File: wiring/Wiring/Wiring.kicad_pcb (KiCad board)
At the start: 2 copper layers, 21 parts, among them U1 MAIN, U2 E, U3 A, U3 B, U3 C, U3 D, U3 F, U3 H, U3 I, U3 J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

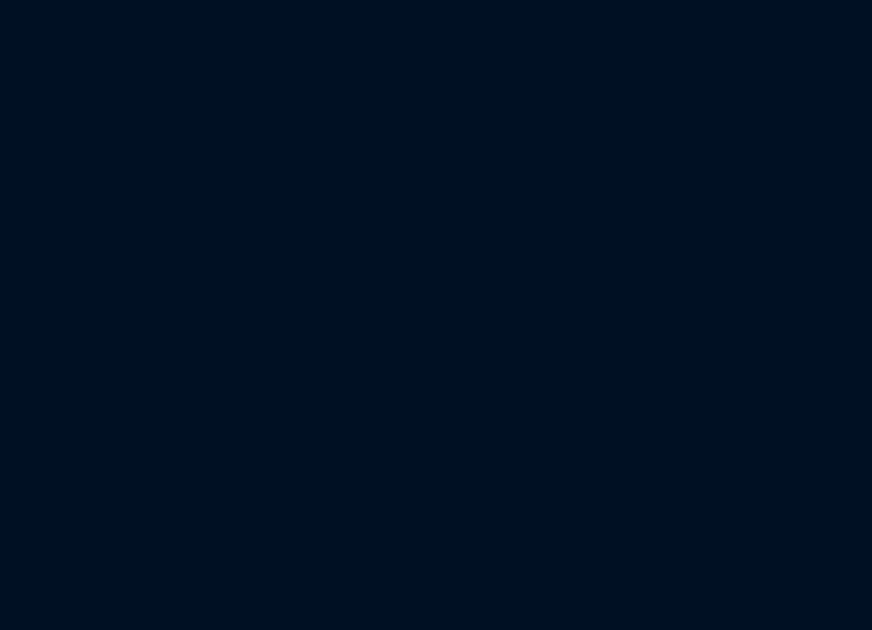
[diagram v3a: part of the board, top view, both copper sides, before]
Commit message: Add U, plus wiring
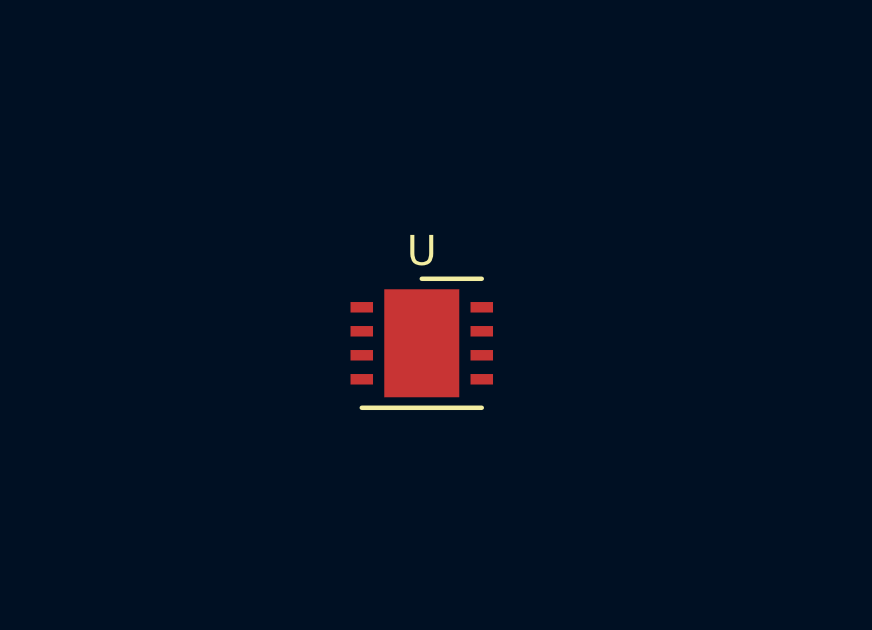
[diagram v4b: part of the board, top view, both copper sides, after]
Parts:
- added U: U, Package_DFN_QFN:DFN-8-1EP_4x4mm_P0.8mm_EP2.5x3.6mm, F.Cu at (28.5, 78.2)
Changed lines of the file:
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@@
     (tracks 0)
     (zones 0)
-    (modules 21)
+    (modules 22)
     (nets 27)
   )
@@
   )
   (module Package_DFN_QFN:DFN-8-1EP_4x4mm_P0.8mm_EP2.5x3.6mm (layer F.Cu)
+    (at 28.48 78.2)
+    (descr "8-Lead Plastic Dual Flat, No Lead Package (MD) - 4x4x0.9 mm Body [DFN] (see Microchip Packaging Specification 00000049BS.pdf)")
+    (tags "DFN 0.8")
+    (attr smd)
+    (fp_text reference U (at 0 -3.075) (layer F.SilkS)
+      (effects (font (size 1 1) (thickness 0.15)))
+    )
+    (fp_text value U (at 0 3.075) (layer F.Fab)
+      (effects (font (size 1 1) (thickness 0.15)))
+    )
+    (fp_line (start 0 -2.15) (end 2 -2.15) (layer F.SilkS) (width 0.15))
+    (fp_line (start -2 2.15) (end 2 2.15) (layer F.SilkS) (width 0.15))
+    (fp_line (start -2.65 2.35) (end 2.65 2.35) (layer F.CrtYd) (width 0.05))
+    (fp_line (start -2.65 -2.35) (end 2.65 -2.35) (layer F.CrtYd) (width 0.05))
+    (fp_line (start 2.65 -2.35) (end 2.65 2.35) (layer F.CrtYd) (width 0.05))
+    (fp_line (start -2.65 -2.35) (end -2.65 2.35) (layer F.CrtYd) (width 0.05))
+    (fp_line (start -2 -1) (end -1 -2) (layer F.Fab) (width 0.15))
+    (fp_line (start -2 2) (end -2 -1) (layer F.Fab) (width 0.15))
+    (fp_line (start 2 2) (end -2 2) (layer F.Fab) (width 0.15))
+    (fp_line (start 2 -2) (end 2 2) (layer F.Fab) (width 0.15))
+    (fp_line (start -1 -2) (end 2 -2) (layer F.Fab) (width 0.15))
+    (fp_text user %R (at 0 0) (layer F.Fab)
+      (effects (font (size 1 1) (thickness 0.15)))
+    )
+    (pad 1 smd rect (at -2 -1.2) (size 0.75 0.35) (layers F.Cu F.Paste F.Mask))
+    (pad 2 smd rect (at -2 -0.4) (size 0.75 0.35) (layers F.Cu F.Paste F.Mask))
+    (pad 3 smd rect (at -2 0.4) (size 0.75 0.35) (layers F.Cu F.Paste F.Mask))
+    (pad 4 smd rect (at -2 1.2) (size 0.75 0.35) (layers F.Cu F.Paste F.Mask))
+    (pad 5 smd rect (at 2 1.2) (size 0.75 0.35) (layers F.Cu F.Paste F.Mask))
+    (pad 6 smd rect (at 2 0.4) (size 0.75 0.35) (layers F.Cu F.Paste F.Mask))
+    (pad 7 smd rect (at 2 -0.4) (size 0.75 0.35) (layers F.Cu F.Paste F.Mask))
+    (pad 8 smd rect (at 2 -1.2) (size 0.75 0.35) (layers F.Cu F.Paste F.Mask))
+    (pad "" smd rect (at -0.625 -1.2) (size 1 1) (layers F.Paste))
+    (pad 9 smd rect (at 0 0) (size 2.5 3.6) (layers F.Cu F.Mask))
+    (pad "" smd rect (at 0.625 -1.2) (size 1 1) (layers F.Paste))
+    (pad "" smd rect (at 0.625 0) (size 1 1) (layers F.Paste))
+    (pad "" smd rect (at -0.625 0) (size 1 1) (layers F.Paste))
+    (pad "" smd rect (at 0.625 1.2) (size 1 1) (layers F.Paste))
+    (pad "" smd rect (at -0.625 1.2) (size 1 1) (layers F.Paste))
+    (model ${KISYS3DMOD}/Package_DFN_QFN.3dshapes/DFN-8-1EP_4x4mm_P0.8mm_EP2.5x3.6mm.wrl
+      (at (xyz 0 0 0))
+      (scale (xyz 1 1 1))
+      (rotate (xyz 0 0 0))
+    )
+  )
+  (module Package_DFN_QFN:DFN-8-1EP_4x4mm_P0.8mm_EP2.5x3.6mm (layer F.Cu)

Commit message: Add V
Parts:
- added U: V, Package_DFN_QFN:DFN-8-1EP_4x4mm_P0.8mm_EP2.5x3.6mm, F.Cu at (186.0, 111.2)
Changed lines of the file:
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@@
   (general
     (thickness 1.6)
-    (drawings 50)
+    (drawings 55)
     (tracks 0)
     (zones 0)
-    (modules 22)
+    (modules 23)
     (nets 27)
   )
@@
   )
   (module Package_DFN_QFN:DFN-8-1EP_4x4mm_P0.8mm_EP2.5x3.6mm (layer F.Cu)
+    (at 185.96 111.22)
+    (descr "8-Lead Plastic Dual Flat, No Lead Package (MD) - 4x4x0.9 mm Body [DFN] (see Microchip Packaging Specification 00000049BS.pdf)")
+    (tags "DFN 0.8")
+    (attr smd)
+    (fp_text reference U (at 0 -3.075) (layer F.SilkS)
+      (effects (font (size 1 1) (thickness 0.15)))
+    )
+    (fp_text value V (at 0 3.075) (layer F.Fab)
+      (effects (font (size 1 1) (thickness 0.15)))
+    )
+    (fp_line (start 0 -2.15) (end 2 -2.15) (layer F.SilkS) (width 0.15))
+    (fp_line (start -2 2.15) (end 2 2.15) (layer F.SilkS) (width 0.15))
+    (fp_line (start -2.65 2.35) (end 2.65 2.35) (layer F.CrtYd) (width 0.05))
+    (fp_line (start -2.65 -2.35) (end 2.65 -2.35) (layer F.CrtYd) (width 0.05))
+    (fp_line (start 2.65 -2.35) (end 2.65 2.35) (layer F.CrtYd) (width 0.05))
+    (fp_line (start -2.65 -2.35) (end -2.65 2.35) (layer F.CrtYd) (width 0.05))
+    (fp_line (start -2 -1) (end -1 -2) (layer F.Fab) (width 0.15))
+    (fp_line (start -2 2) (end -2 -1) (layer F.Fab) (width 0.15))
+    (fp_line (start 2 2) (end -2 2) (layer F.Fab) (width 0.15))
+    (fp_line (start 2 -2) (end 2 2) (layer F.Fab) (width 0.15))
+    (fp_line (start -1 -2) (end 2 -2) (layer F.Fab) (width 0.15))
+    (fp_text user %R (at 0 0) (layer F.Fab)
+      (effects (font (size 1 1) (thickness 0.15)))
+    )
+    (pad 1 smd rect (at -2 -1.2) (size 0.75 0.35) (layers F.Cu F.Paste F.Mask))
+    (pad 2 smd rect (at -2 -0.4) (size 0.75 0.35) (layers F.Cu F.Paste F.Mask))
+    (pad 3 smd rect (at -2 0.4) (size 0.75 0.35) (layers F.Cu F.Paste F.Mask))
+    (pad 4 smd rect (at -2 1.2) (size 0.75 0.35) (layers F.Cu F.Paste F.Mask))
+    (pad 5 smd rect (at 2 1.2) (size 0.75 0.35) (layers F.Cu F.Paste F.Mask))
+    (pad 6 smd rect (at 2 0.4) (size 0.75 0.35) (layers F.Cu F.Paste F.Mask))
+    (pad 7 smd rect (at 2 -0.4) (size 0.75 0.35) (layers F.Cu F.Paste F.Mask))
+    (pad 8 smd rect (at 2 -1.2) (size 0.75 0.35) (layers F.Cu F.Paste F.Mask))
+    (pad "" smd rect (at -0.625 -1.2) (size 1 1) (layers F.Paste))
+    (pad 9 smd rect (at 0 0) (size 2.5 3.6) (layers F.Cu F.Mask))
+    (pad "" smd rect (at 0.625 -1.2) (size 1 1) (layers F.Paste))
+    (pad "" smd rect (at 0.625 0) (size 1 1) (layers F.Paste))
+    (pad "" smd rect (at -0.625 0) (size 1 1) (layers F.Paste))
+    (pad "" smd rect (at 0.625 1.2) (size 1 1) (layers F.Paste))
+    (pad "" smd rect (at -0.625 1.2) (size 1 1) (layers F.Paste))
+    (model ${KISYS3DMOD}/Package_DFN_QFN.3dshapes/DFN-8-1EP_4x4mm_P0.8mm_EP2.5x3.6mm.wrl
+      (at (xyz 0 0 0))
+      (scale (xyz 1 1 1))
+      (rotate (xyz 0 0 0))
+    )
+  )
+  (module Package_DFN_QFN:DFN-8-1EP_4x4mm_P0.8mm_EP2.5x3.6mm (layer F.Cu)
     (at 28.48 78.2)
     (descr "8-Lead Plastic Dual Flat, No Lead Package (MD) - 4x4x0.9 mm Body [DFN] (see Microchip Packaging Specification 00000049BS.pdf)")
@@
     )
   )
+  (gr_line (start 27.94 68.58) (end 27.94 78.74) (layer Cmts.User) (width 0.15))
+  (gr_line (start 170.18 114.3) (end 170.18 109.22) (layer Cmts.User) (width 0.15))
+  (gr_line (start 203.2 114.3) (end 170.18 114.3) (layer Cmts.User) (width 0.15))
+  (gr_line (start 203.2 109.22) (end 203.2 114.3) (layer Cmts.User) (width 0.15))
+  (gr_line (start 170.18 109.22) (end 203.2 109.22) (layer Cmts.User) (width 0.15))
   (gr_line (start 149.86 137.16) (end 149.86 132.08) (layer Cmts.User) (width 0.15))
   (gr_line (start 162.56 137.16) (end 149.86 137.16) (layer Cmts.User) (width 0.15))

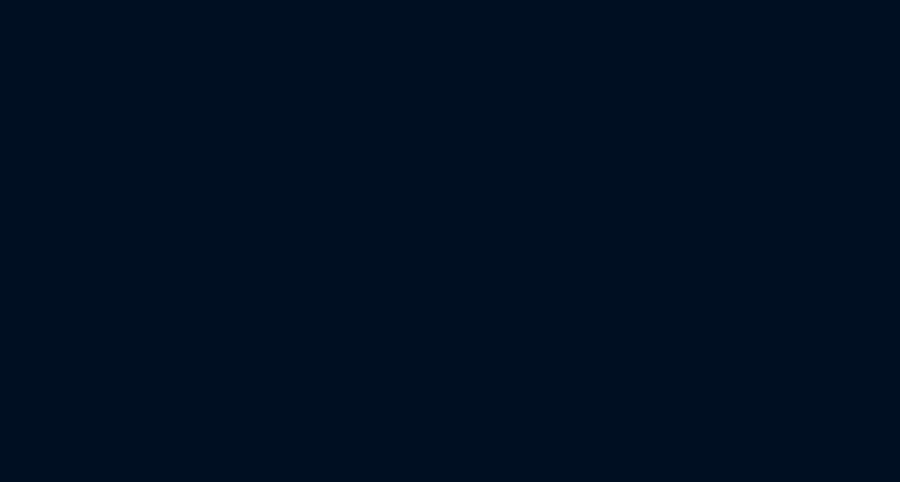
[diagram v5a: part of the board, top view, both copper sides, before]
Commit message: Add computer lab outlet: W
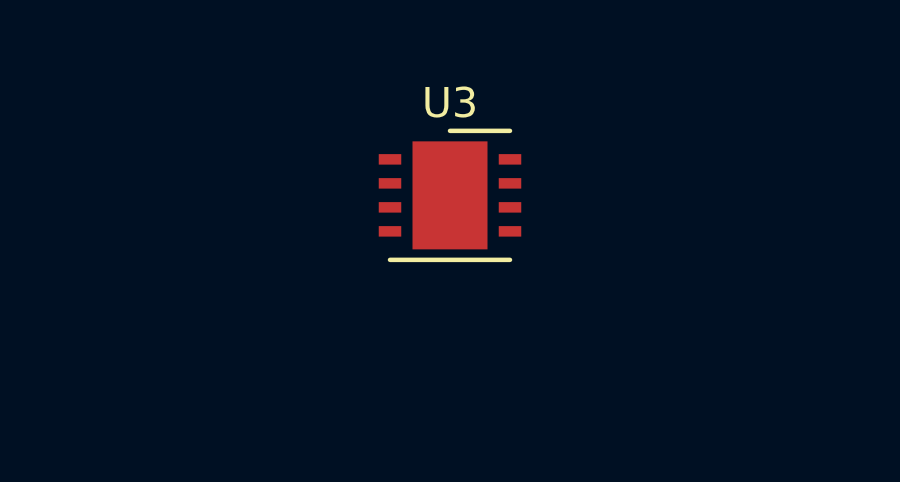
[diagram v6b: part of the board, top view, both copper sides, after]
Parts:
- added U3: W, Package_DFN_QFN:DFN-8-1EP_4x4mm_P0.8mm_EP2.5x3.6mm, F.Cu at (211.4, 47.9)

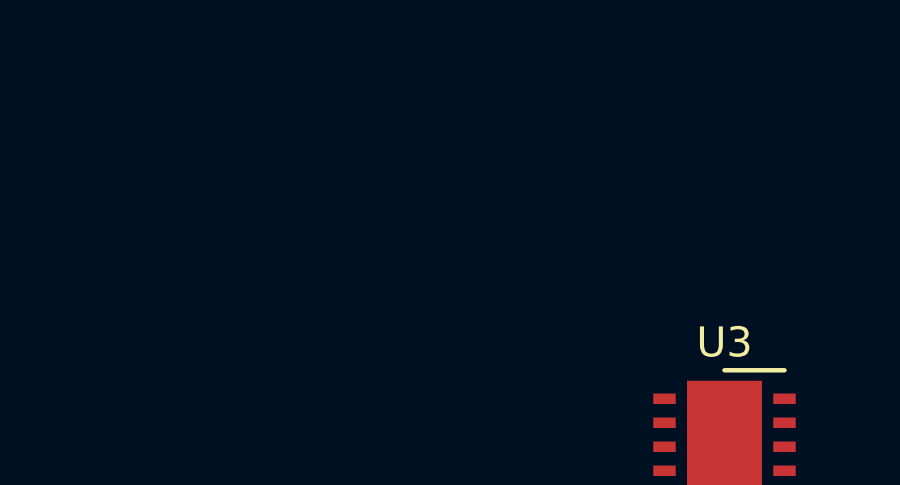
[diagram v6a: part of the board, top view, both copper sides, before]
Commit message: Add outlet X: Front table
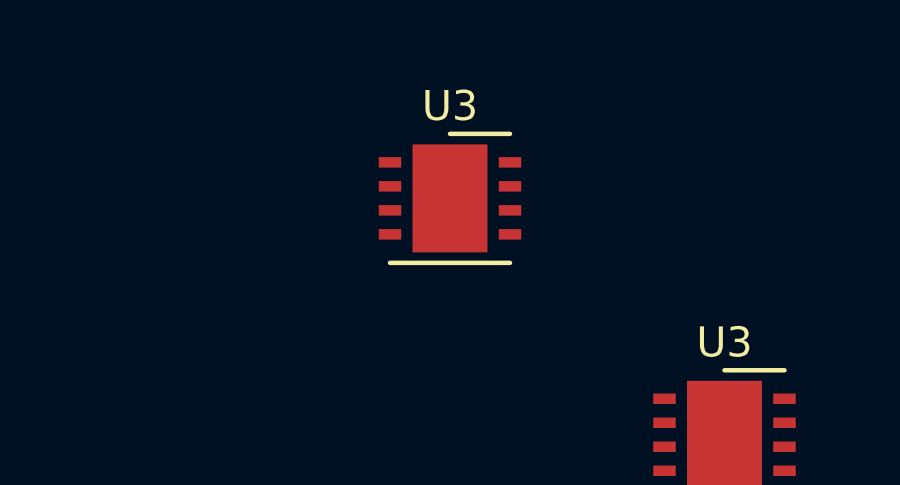
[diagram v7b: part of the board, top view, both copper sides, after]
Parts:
- added U3: X, Package_DFN_QFN:DFN-8-1EP_4x4mm_P0.8mm_EP2.5x3.6mm, F.Cu at (119.1, 48.0)
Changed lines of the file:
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@@
     (tracks 0)
     (zones 0)
-    (modules 24)
+    (modules 25)
     (nets 27)
   )
@@
   )
   (module Package_DFN_QFN:DFN-8-1EP_4x4mm_P0.8mm_EP2.5x3.6mm (layer F.Cu)
+    (at 119.12 48)
+    (descr "8-Lead Plastic Dual Flat, No Lead Package (MD) - 4x4x0.9 mm Body [DFN] (see Microchip Packaging Specification 00000049BS.pdf)")
+    (tags "DFN 0.8")
+    (attr smd)
+    (fp_text reference U3 (at 0 -3.075) (layer F.SilkS)
+      (effects (font (size 1 1) (thickness 0.15)))
+    )
+    (fp_text value X (at 0 3.075) (layer F.Fab)
+      (effects (font (size 1 1) (thickness 0.15)))
+    )
+    (fp_line (start -1 -2) (end 2 -2) (layer F.Fab) (width 0.15))
+    (fp_line (start 2 -2) (end 2 2) (layer F.Fab) (width 0.15))
+    (fp_line (start 2 2) (end -2 2) (layer F.Fab) (width 0.15))
+    (fp_line (start -2 2) (end -2 -1) (layer F.Fab) (width 0.15))
+    (fp_line (start -2 -1) (end -1 -2) (layer F.Fab) (width 0.15))
+    (fp_line (start -2.65 -2.35) (end -2.65 2.35) (layer F.CrtYd) (width 0.05))
+    (fp_line (start 2.65 -2.35) (end 2.65 2.35) (layer F.CrtYd) (width 0.05))
+    (fp_line (start -2.65 -2.35) (end 2.65 -2.35) (layer F.CrtYd) (width 0.05))
+    (fp_line (start -2.65 2.35) (end 2.65 2.35) (layer F.CrtYd) (width 0.05))
+    (fp_line (start -2 2.15) (end 2 2.15) (layer F.SilkS) (width 0.15))
+    (fp_line (start 0 -2.15) (end 2 -2.15) (layer F.SilkS) (width 0.15))
+    (fp_text user %R (at 0 0) (layer F.Fab)
+      (effects (font (size 1 1) (thickness 0.15)))
+    )
+    (pad 1 smd rect (at -2 -1.2) (size 0.75 0.35) (layers F.Cu F.Paste F.Mask))
+    (pad 2 smd rect (at -2 -0.4) (size 0.75 0.35) (layers F.Cu F.Paste F.Mask))
+    (pad 3 smd rect (at -2 0.4) (size 0.75 0.35) (layers F.Cu F.Paste F.Mask))
+    (pad 4 smd rect (at -2 1.2) (size 0.75 0.35) (layers F.Cu F.Paste F.Mask))
+    (pad 5 smd rect (at 2 1.2) (size 0.75 0.35) (layers F.Cu F.Paste F.Mask))
+    (pad 6 smd rect (at 2 0.4) (size 0.75 0.35) (layers F.Cu F.Paste F.Mask))
+    (pad 7 smd rect (at 2 -0.4) (size 0.75 0.35) (layers F.Cu F.Paste F.Mask))
+    (pad 8 smd rect (at 2 -1.2) (size 0.75 0.35) (layers F.Cu F.Paste F.Mask))
+    (pad "" smd rect (at -0.625 -1.2) (size 1 1) (layers F.Paste))
+    (pad 9 smd rect (at 0 0) (size 2.5 3.6) (layers F.Cu F.Mask))
+    (pad "" smd rect (at 0.625 -1.2) (size 1 1) (layers F.Paste))
+    (pad "" smd rect (at 0.625 0) (size 1 1) (layers F.Paste))
+    (pad "" smd rect (at -0.625 0) (size 1 1) (layers F.Paste))
+    (pad "" smd rect (at 0.625 1.2) (size 1 1) (layers F.Paste))
+    (pad "" smd rect (at -0.625 1.2) (size 1 1) (layers F.Paste))
+    (model ${KISYS3DMOD}/Package_DFN_QFN.3dshapes/DFN-8-1EP_4x4mm_P0.8mm_EP2.5x3.6mm.wrl
+      (at (xyz 0 0 0))
+      (scale (xyz 1 1 1))
+      (rotate (xyz 0 0 0))
+    )
+  )
+  (module Package_DFN_QFN:DFN-8-1EP_4x4mm_P0.8mm_EP2.5x3.6mm (layer F.Cu)

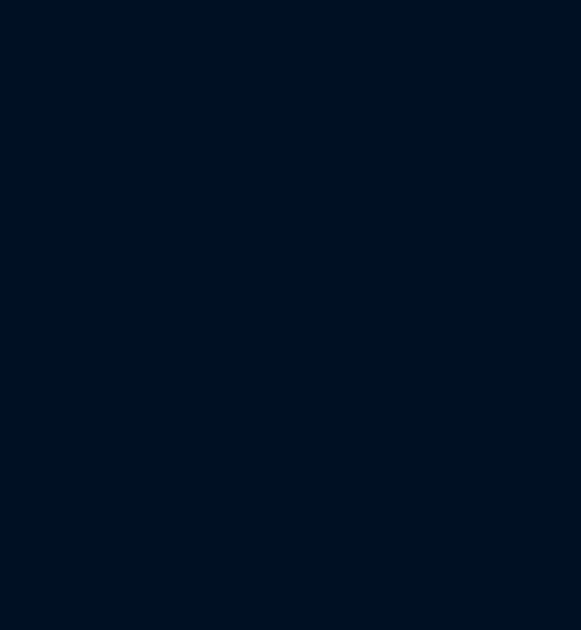
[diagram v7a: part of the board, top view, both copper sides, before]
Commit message: Add outlet Y: workbench
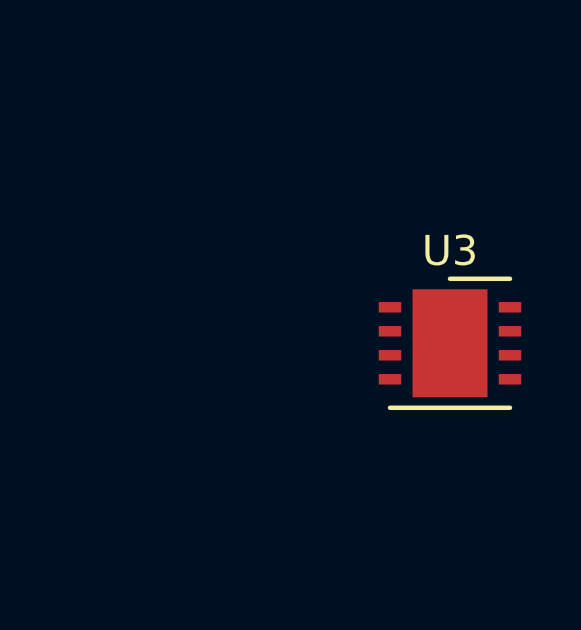
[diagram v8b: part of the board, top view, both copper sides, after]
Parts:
- added U3: Y, Package_DFN_QFN:DFN-8-1EP_4x4mm_P0.8mm_EP2.5x3.6mm, F.Cu at (277.9, 58.9)
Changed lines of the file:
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@@
     (tracks 0)
     (zones 0)
-    (modules 25)
+    (modules 26)
     (nets 27)
   )
@@
   )
   (module Package_DFN_QFN:DFN-8-1EP_4x4mm_P0.8mm_EP2.5x3.6mm (layer F.Cu)
+    (at 277.9 58.9)
+    (descr "8-Lead Plastic Dual Flat, No Lead Package (MD) - 4x4x0.9 mm Body [DFN] (see Microchip Packaging Specification 00000049BS.pdf)")
+    (tags "DFN 0.8")
+    (attr smd)
+    (fp_text reference U3 (at 0 -3.075) (layer F.SilkS)
+      (effects (font (size 1 1) (thickness 0.15)))
+    )
+    (fp_text value Y (at 0 3.075) (layer F.Fab)
+      (effects (font (size 1 1) (thickness 0.15)))
+    )
+    (fp_line (start -1 -2) (end 2 -2) (layer F.Fab) (width 0.15))
+    (fp_line (start 2 -2) (end 2 2) (layer F.Fab) (width 0.15))
+    (fp_line (start 2 2) (end -2 2) (layer F.Fab) (width 0.15))
+    (fp_line (start -2 2) (end -2 -1) (layer F.Fab) (width 0.15))
+    (fp_line (start -2 -1) (end -1 -2) (layer F.Fab) (width 0.15))
+    (fp_line (start -2.65 -2.35) (end -2.65 2.35) (layer F.CrtYd) (width 0.05))
+    (fp_line (start 2.65 -2.35) (end 2.65 2.35) (layer F.CrtYd) (width 0.05))
+    (fp_line (start -2.65 -2.35) (end 2.65 -2.35) (layer F.CrtYd) (width 0.05))
+    (fp_line (start -2.65 2.35) (end 2.65 2.35) (layer F.CrtYd) (width 0.05))
+    (fp_line (start -2 2.15) (end 2 2.15) (layer F.SilkS) (width 0.15))
+    (fp_line (start 0 -2.15) (end 2 -2.15) (layer F.SilkS) (width 0.15))
+    (fp_text user %R (at 0 0) (layer F.Fab)
+      (effects (font (size 1 1) (thickness 0.15)))
+    )
+    (pad 1 smd rect (at -2 -1.2) (size 0.75 0.35) (layers F.Cu F.Paste F.Mask))
+    (pad 2 smd rect (at -2 -0.4) (size 0.75 0.35) (layers F.Cu F.Paste F.Mask))
+    (pad 3 smd rect (at -2 0.4) (size 0.75 0.35) (layers F.Cu F.Paste F.Mask))
+    (pad 4 smd rect (at -2 1.2) (size 0.75 0.35) (layers F.Cu F.Paste F.Mask))
+    (pad 5 smd rect (at 2 1.2) (size 0.75 0.35) (layers F.Cu F.Paste F.Mask))
+    (pad 6 smd rect (at 2 0.4) (size 0.75 0.35) (layers F.Cu F.Paste F.Mask))
+    (pad 7 smd rect (at 2 -0.4) (size 0.75 0.35) (layers F.Cu F.Paste F.Mask))
+    (pad 8 smd rect (at 2 -1.2) (size 0.75 0.35) (layers F.Cu F.Paste F.Mask))
+    (pad "" smd rect (at -0.625 -1.2) (size 1 1) (layers F.Paste))
+    (pad 9 smd rect (at 0 0) (size 2.5 3.6) (layers F.Cu F.Mask))
+    (pad "" smd rect (at 0.625 -1.2) (size 1 1) (layers F.Paste))
+    (pad "" smd rect (at 0.625 0) (size 1 1) (layers F.Paste))
+    (pad "" smd rect (at -0.625 0) (size 1 1) (layers F.Paste))
+    (pad "" smd rect (at 0.625 1.2) (size 1 1) (layers F.Paste))
+    (pad "" smd rect (at -0.625 1.2) (size 1 1) (layers F.Paste))
+    (model ${KISYS3DMOD}/Package_DFN_QFN.3dshapes/DFN-8-1EP_4x4mm_P0.8mm_EP2.5x3.6mm.wrl
+      (at (xyz 0 0 0))
+      (scale (xyz 1 1 1))
+      (rotate (xyz 0 0 0))
+    )
+  )
+  (module Package_DFN_QFN:DFN-8-1EP_4x4mm_P0.8mm_EP2.5x3.6mm (layer F.Cu)
